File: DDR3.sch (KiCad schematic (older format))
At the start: 48 parts, among them U15 MT41K256M16HA-125_E, U16 MT41K256M16HA-125_E, U8 xc7z020clg400

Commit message: random updates
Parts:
- removed U8: xc7z020clg400, DFTcustom:BGA400_0.8p_17mmx17mm, symbol DFTBoard-rescue:xc7z020clg400-
- added U20: xc7z020clg484, DFTcustom:BGA-484_19.0x19.0mm_Layout22x22_P0.80mm_dia0.40mm, symbol xilinx7:xc7z020clg484
- C100, C101, C102, C103, C104, C105, C106, C93, C94, C95, C96, C97, C98: footprint Capacitor_SMD:C_0603_1608Metric -> Capacitor_SMD:C_0402_1005Metric
- R47, R48, R50: footprint Resistors_SMD:R_0402 -> Resistor_SMD:R_0402_1005Metric
- R51, R52, R53, R54, R55, R56, R57, R58, R59, R60, R61, R62, R63, R64, R65, R66, R67, R68, R69, R70, R71, R72, R73: footprint Resistor_SMD:R_0201_0603Metric -> Resistor_SMD:R_0402_1005Metric
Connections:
- net +1V35: now also U20.E2 (VCCO_DDR_502[9]), U20.F5 (VCCO_DDR_502[9]), U20.H1 (VCCO_DDR_502[9]), U20.J4 (VCCO_DDR_502[9]), U20.K7 (VCCO_DDR_502[9]), U20.M3 (VCCO_DDR_502[9]), U20.N6 (VCCO_DDR_502[9]), U20.R2 (VCCO_DDR_502[9]), U20.V1 (VCCO_DDR_502[9])
- net DDR3_A0: now also U20.M4 (PS_DDR_A0_502)
- net DDR3_A1: now also U20.M5 (PS_DDR_A1_502)
- net DDR3_A10: now also U20.J3 (PS_DDR_A10_502)
- net DDR3_A11: now also U20.G5 (PS_DDR_A11_502)
- net DDR3_A12: now also U20.H4 (PS_DDR_A12_502)
- net DDR3_A13: now also U20.F4 (PS_DDR_A13_502)
- net DDR3_A14: now also U20.G4 (PS_DDR_A14_502)
- net DDR3_A2: now also U20.K4 (PS_DDR_A2_502)
- net DDR3_A3: now also U20.L4 (PS_DDR_A3_502)
- net DDR3_A4: now also U20.K6 (PS_DDR_A4_502)
- net DDR3_A5: now also U20.K5 (PS_DDR_A5_502)
- net DDR3_A6: now also U20.J7 (PS_DDR_A6_502)
- net DDR3_A7: now also U20.J6 (PS_DDR_A7_502)
- net DDR3_A8: now also U20.J5 (PS_DDR_A8_502)
- net DDR3_A9: now also U20.H5 (PS_DDR_A9_502)
- net DDR3_BA0: now also U20.L7 (PS_DDR_BA0_502)
- net DDR3_BA1: now also U20.L6 (PS_DDR_BA1_502)
- net DDR3_BA2: now also U20.M6 (PS_DDR_BA2_502)
- net DDR3_CAS#: now also U20.P3 (PS_DDR_CAS_B_502)
- net DDR3_CKE: now also U20.V3 (PS_DDR_CKE_502)
- net DDR3_CK_N: now also U20.N5 (PS_DDR_CKN_502)
- net DDR3_CK_P: now also U20.N4 (PS_DDR_CKP_502)
- net DDR3_CS#: now also U20.P6 (PS_DDR_CS_B_502)
- net DDR3_DM0: now also U20.B1 (PS_DDR_DM0_502)
- net DDR3_DM1: now also U20.H3 (PS_DDR_DM1_502)
- net DDR3_DM2: now also U20.P1 (PS_DDR_DM2_502)
- net DDR3_DM3: now also U20.AA2 (PS_DDR_DM3_502)
- net DDR3_DQ0: now also U20.D1 (PS_DDR_DQ0_502)
- net DDR3_DQ1: now also U20.C3 (PS_DDR_DQ1_502)
- net DDR3_DQ10: now also U20.L1 (PS_DDR_DQ10_502)
- net DDR3_DQ11: now also U20.L2 (PS_DDR_DQ11_502)
- net DDR3_DQ12: now also U20.L3 (PS_DDR_DQ12_502)
- net DDR3_DQ13: now also U20.K1 (PS_DDR_DQ13_502)
- net DDR3_DQ14: now also U20.J1 (PS_DDR_DQ14_502)
- net DDR3_DQ15: now also U20.K3 (PS_DDR_DQ15_502)
- net DDR3_DQ16: now also U20.M1 (PS_DDR_DQ16_502)
- net DDR3_DQ17: now also U20.T3 (PS_DDR_DQ17_502)
- net DDR3_DQ18: now also U20.N3 (PS_DDR_DQ18_502)
- net DDR3_DQ19: now also U20.T1 (PS_DDR_DQ19_502)
- net DDR3_DQ2: now also U20.B2 (PS_DDR_DQ2_502)
- net DDR3_DQ20: now also U20.R3 (PS_DDR_DQ20_502)
- net DDR3_DQ21: now also U20.T2 (PS_DDR_DQ21_502)
- net DDR3_DQ22: now also U20.M2 (PS_DDR_DQ22_502)
- net DDR3_DQ23: now also U20.R1 (PS_DDR_DQ23_502)
- net DDR3_DQ24: now also U20.AA3 (PS_DDR_DQ24_502)
- net DDR3_DQ25: now also U20.U1 (PS_DDR_DQ25_502)
- net DDR3_DQ26: now also U20.AA1 (PS_DDR_DQ26_502)
- net DDR3_DQ27: now also U20.U2 (PS_DDR_DQ27_502)
- net DDR3_DQ28: now also U20.W1 (PS_DDR_DQ28_502)
- net DDR3_DQ29: now also U20.Y3 (PS_DDR_DQ29_502)
- net DDR3_DQ3: now also U20.D3 (PS_DDR_DQ3_502)
- net DDR3_DQ30: now also U20.W3 (PS_DDR_DQ30_502)
- net DDR3_DQ31: now also U20.Y1 (PS_DDR_DQ31_502)
- net DDR3_DQ4: now also U20.E3 (PS_DDR_DQ4_502)
- net DDR3_DQ5: now also U20.E1 (PS_DDR_DQ5_502)
- net DDR3_DQ6: now also U20.F2 (PS_DDR_DQ6_502)
- net DDR3_DQ7: now also U20.F1 (PS_DDR_DQ7_502)
- net DDR3_DQ8: now also U20.G2 (PS_DDR_DQ8_502)
- net DDR3_DQ9: now also U20.G1 (PS_DDR_DQ9_502)
- net DDR3_DQS0_N: now also U20.D2 (PS_DDR_DQS_N0_502)
- net DDR3_DQS0_P: now also U20.C2 (PS_DDR_DQS_P0_502)
- net DDR3_DQS1_N: now also U20.J2 (PS_DDR_DQS_N1_502)
- net DDR3_DQS1_P: now also U20.H2 (PS_DDR_DQS_P1_502)
- net DDR3_DQS2_N: now also U20.P2 (PS_DDR_DQS_N2_502)
- net DDR3_DQS2_P: now also U20.N2 (PS_DDR_DQS_P2_502)
- net DDR3_DQS3_N: now also U20.W2 (PS_DDR_DQS_N3_502)
- net DDR3_DQS3_P: now also U20.V2 (PS_DDR_DQS_P3_502)
- net DDR3_DRST#: now also U20.F3 (PS_DDR_DRST_B_502)
- net DDR3_ODT: now also U20.P5 (PS_DDR_ODT_502)
- net DDR3_RAS#: now also U20.R5 (PS_DDR_RAS_B_502)
- net DDR3_WE#: now also U20.R4 (PS_DDR_WE_B_502)
- net VREF: now also U20.H7 (PS_DDR_VREF0_502), U20.P7 (PS_DDR_VREF1_502)
- net at R75.1: now also U20.M7 (PS_DDR_VRN_502)
- net at R76.1: now also U20.N7 (PS_DDR_VRP_502)
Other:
- note added: "1066 Mb/s (533 Hz)\nShould be attainable by all \nspeed grades of Zynq\nthrough the PS DDR interface\nThis precludes use of internal Vref"
- note added: "Todo: DDR Bypass Caps?"
- moved on the sheet: C100, C101, C102, C103, C104, C99

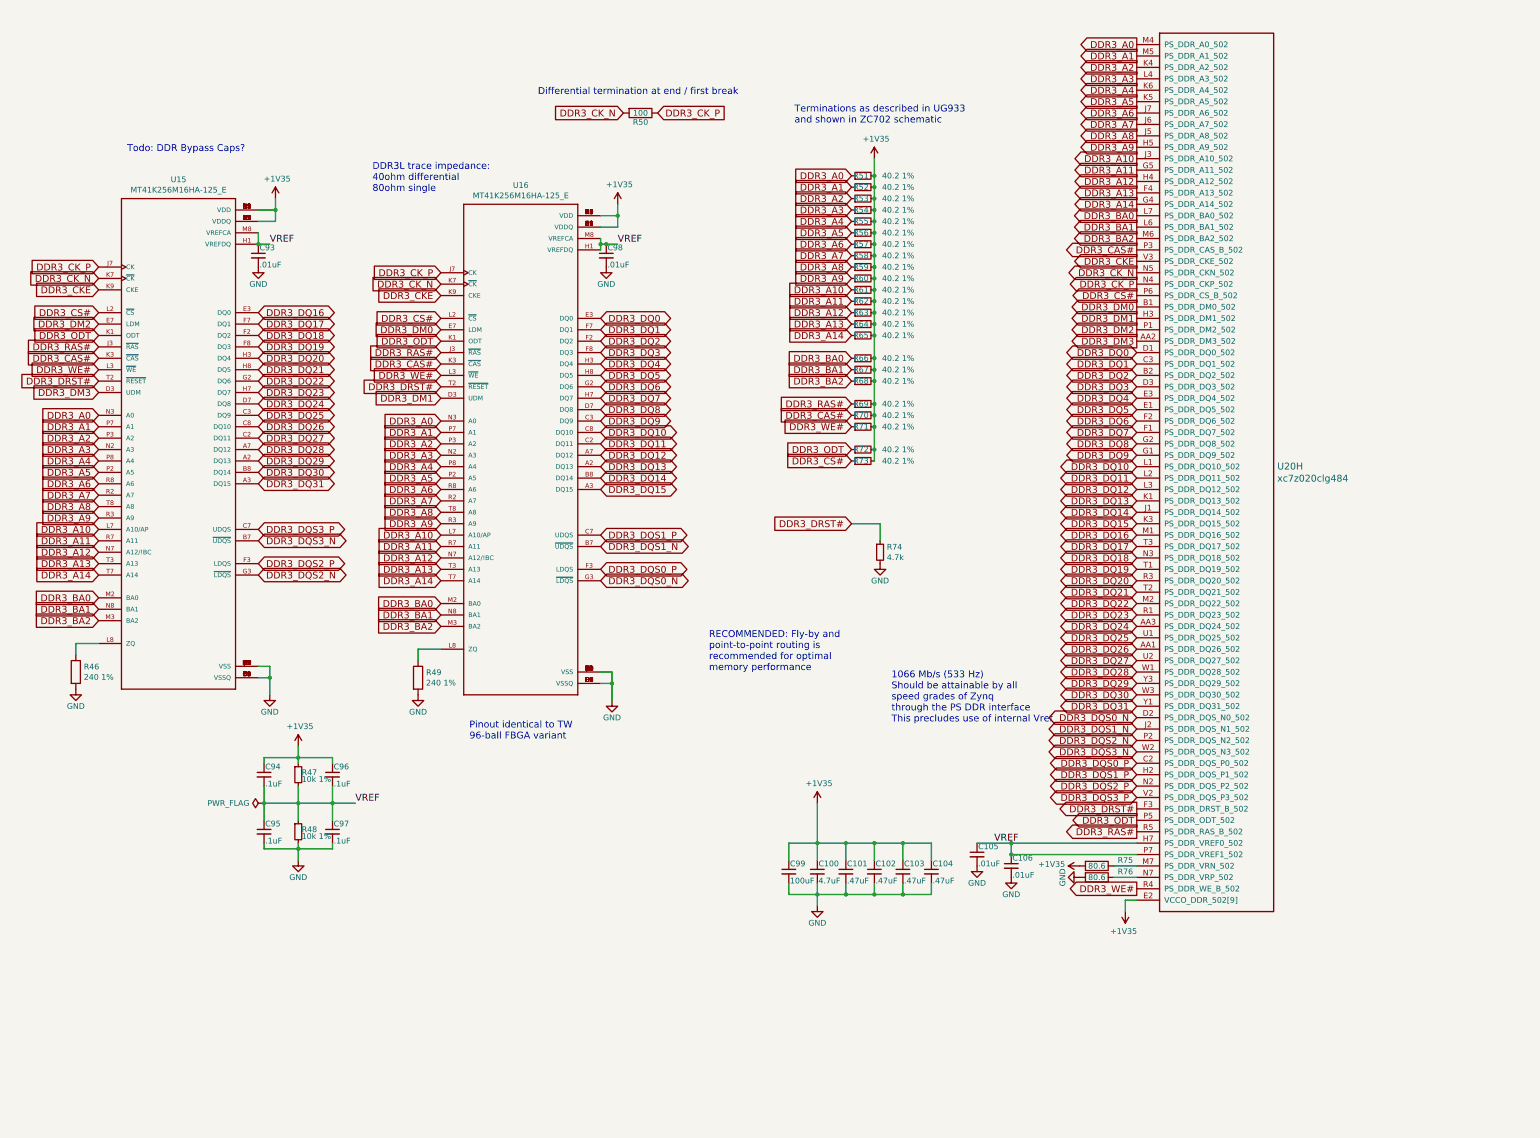
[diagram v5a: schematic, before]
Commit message: everything placed, about to shrink text size globally
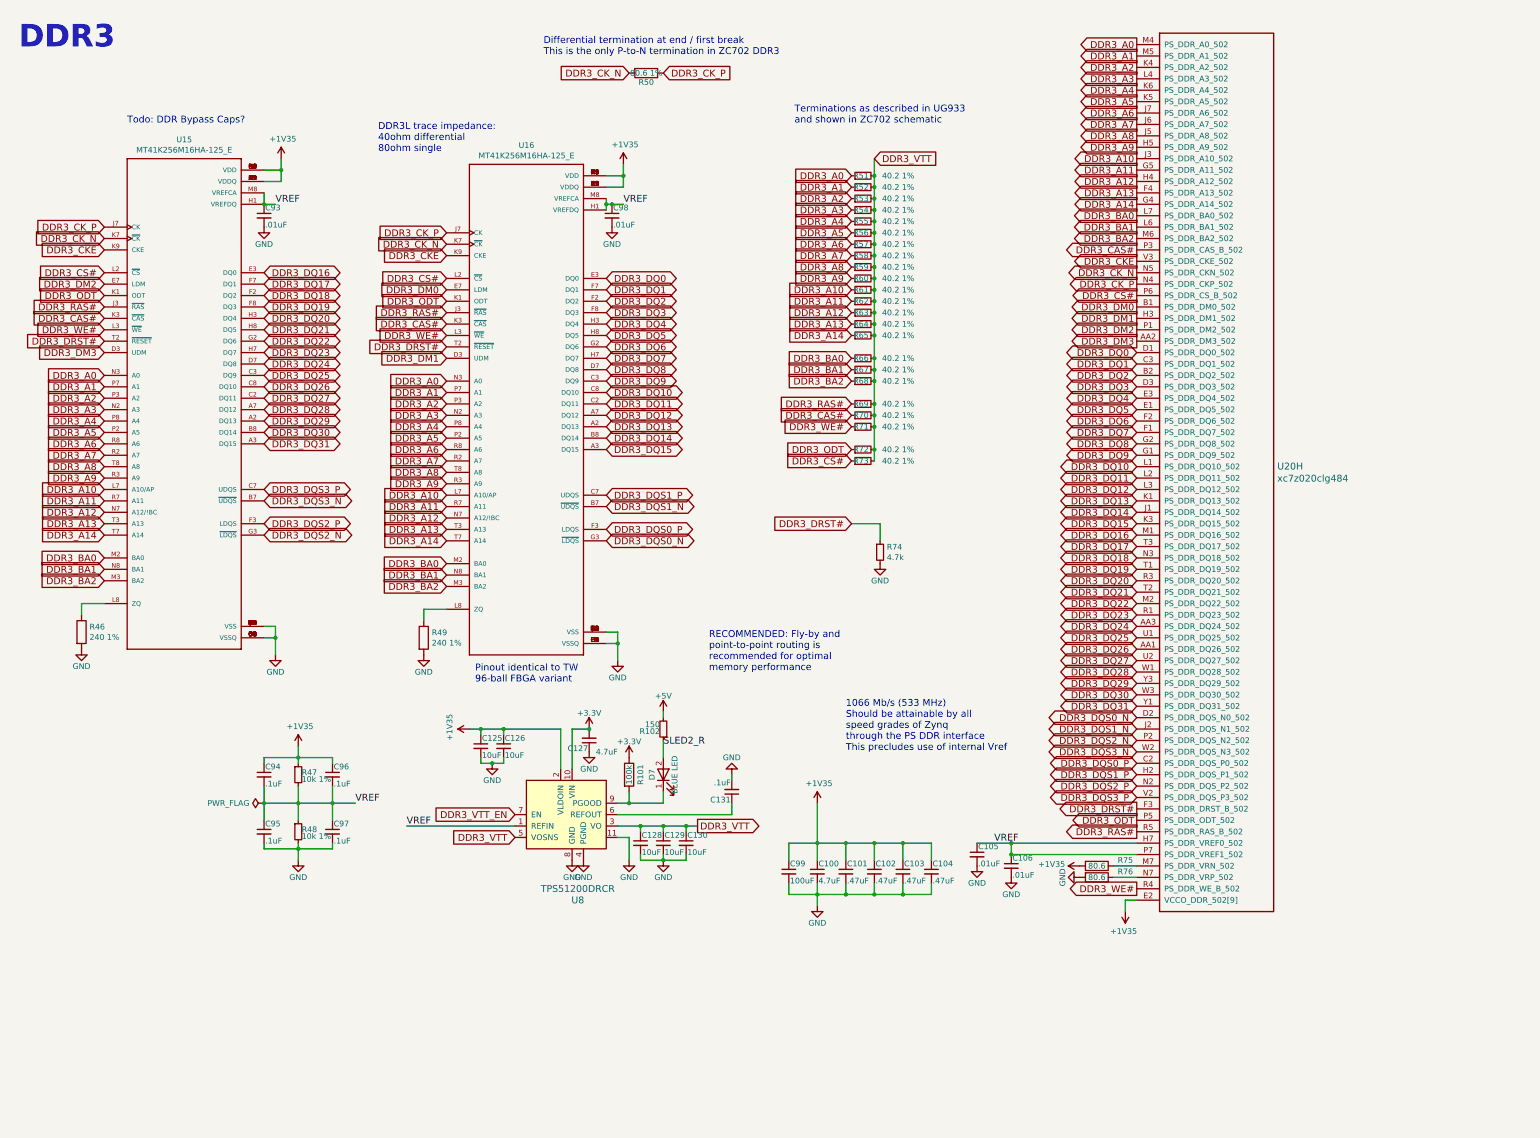
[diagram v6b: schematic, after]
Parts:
- added C125, C126, C128, C129, C130: 10uF, Capacitor_SMD:C_0603_1608Metric, symbol Device:C_Small
- added C127: 4.7uF, Capacitor_SMD:C_0402_1005Metric, symbol Device:C_Small
- added C131: .1uF, Capacitor_SMD:C_0402_1005Metric, symbol Device:C_Small
- added D7: BLUE LED, Capacitor_SMD:C_0603_1608Metric, symbol DFTBoard-rescue:LED-
- added R101: 100k, Resistor_SMD:R_0402_1005Metric, symbol Device:R
- added R102: 150, Resistor_SMD:R_0402_1005Metric, symbol Device:R_Small
- added U8: TPS51200DRCR, Package_SON:VSON-10-1EP_3x3mm_P0.5mm_EP1.65x2.4mm_ThermalVias, symbol tps51200DRCR:TPS51200DRCR
- R50: value 100 -> 80.6 1%; MPN RC0402FR-07100RL -> (none); SPN 311-100LRCT-ND -> (none)
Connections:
- net +1V35: now also C125.1, C126.1, U8.2 (VLDOIN); no longer R51.2, R52.2, R53.2, R54.2, R55.2, R56.2, R57.2, R58.2, R59.2, R60.2, R61.2, R62.2, R63.2, R64.2, R65.2, R66.2, R67.2, R68.2, R69.2, R70.2, R71.2, R72.2, R73.2
- net GND: now also C125.2, C126.2, C127.1, C128.2, C129.2, C130.2, C131.2, U8.11, U8.4 (PGND), U8.8 (GND)
- net VREF: now also U8.1 (REFIN)
- new net: C131.1, U8.6 (REFOUT)
- new net: D7.1 (K), R101.2, U8.9 (PGOOD)
- new net +3V3: C127.2, R101.1, U8.10 (VIN)
- new net +5V: R102.2
- new net DDR3_VTT: C128.1, C129.1, C130.1, R51.2, R52.2, R53.2, R54.2, R55.2, R56.2, R57.2, R58.2, R59.2, R60.2, R61.2, R62.2, R63.2, R64.2, R65.2, R66.2, R67.2, R68.2, R69.2, R70.2, R71.2, R72.2, R73.2, U8.3 (VO), U8.5 (VOSNS)
- new net DDR3_VTT_EN: U8.7 (EN)
- new net SLED2_R: D7.2 (A), R102.1
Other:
- note added: "1066 Mb/s (533 MHz)\nShould be attainable by all \nspeed grades of Zynq\nthrough the PS DDR interface\nThis precludes use of internal Vref"
- note added: "DDR3"
- note added: "Differential termination at end / first break\nThis is the only P-to-N termination in ZC702 DDR3"
- note removed: "1066 Mb/s (533 Hz)\nShould be attainable by all \nspeed grades of Zynq\nthrough the PS DDR interface\nThis precludes use of internal Vref"
- note removed: "Differential termination at end / first break"
- moved on the sheet: C93, C98, R46, R49, R50, U15, U16
